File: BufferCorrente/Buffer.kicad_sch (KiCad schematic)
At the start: 6 parts

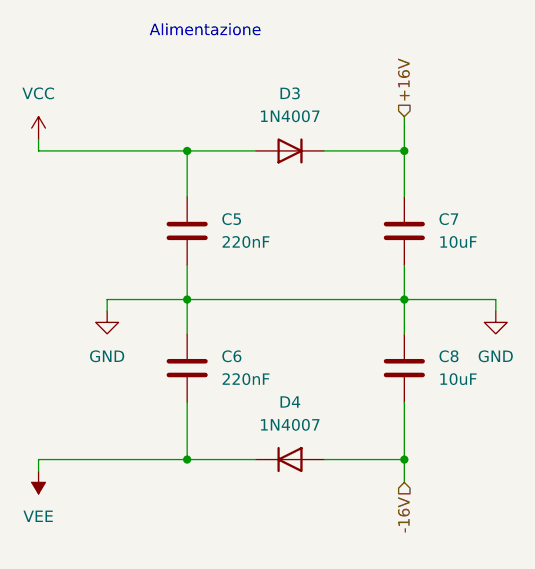
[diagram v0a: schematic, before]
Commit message: Aggiornata la PCB del buffer in corrente con coponenti SMD e groud plane
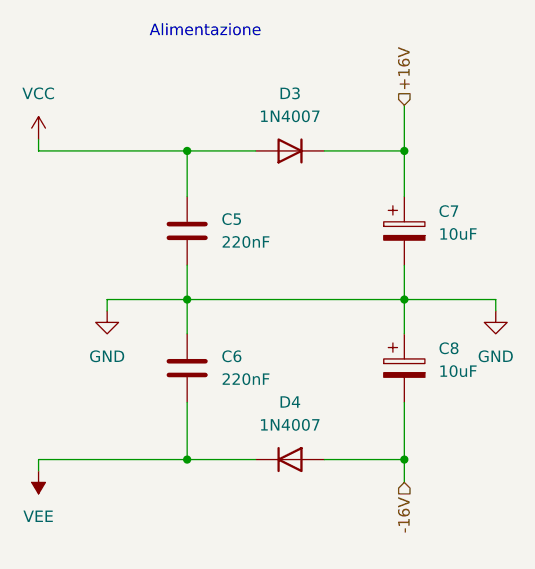
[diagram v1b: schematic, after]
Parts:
- removed C7, C8: 10uF, Capacitor_THT:C_Rect_L7.0mm_W2.0mm_P5.00mm, symbol Device:C
- added C7, C8: 10uF, Capacitor_Tantalum_SMD:CP_EIA-3528-21_Kemet-B, symbol Device:C_Polarized
- C5, C6: footprint Capacitor_THT:C_Rect_L7.0mm_W2.0mm_P5.00mm -> Capacitor_SMD:C_0201_0603Metric
- D3, D4: footprint Diode_THT:D_DO-41_SOD81_P10.16mm_Horizontal -> Diode_SMD:D_SMA
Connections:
- net +16V: now also C7.1
- net -16V: now also C8.2
- net GND: now also C7.2, C8.1
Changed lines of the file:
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@@
 	(wire
 		(pts
-			(xy 156.21 72.39) (xy 156.21 76.2)
+			(xy 156.21 71.12) (xy 156.21 76.2)
 		)
 		(stroke
@@
 		(shape input)
 		(at 156.21 113.03 270)
-		(fields_autoplaced yes)
 		(effects
 			(font
@@
 	(hierarchical_label "+16V"
 		(shape input)
-		(at 156.21 72.39 90)
-		(fields_autoplaced yes)
+		(at 156.21 71.12 90)
 		(effects
 			(font
@@
 	)
 	(symbol
-		(lib_id "Device:C")
+		(lib_id "Device:C_Polarized")
 		(at 156.21 85.09 0)
 		(unit 1)
@@
 		(fields_autoplaced yes)
 		(property "Reference" "C7"
-			(at 160.02 83.8199 0)
+			(at 160.02 82.9309 0)
 			(effects
 				(font
@@
 		)
 		(property "Value" "10uF"
-			(at 160.02 86.3599 0)
+			(at 160.02 85.4709 0)
 			(effects
 				(font
@@
 			)
 		)
-		(property "Footprint" "Capacitor_THT:C_Rect_L7.0mm_W2.0mm_P5.00mm"
+		(property "Footprint" "Capacitor_Tantalum_SMD:CP_EIA-3528-21_Kemet-B"
 			(at 157.1752 88.9 0)
 			(effects
@@
 			)
 		)
-		(property "Description" "Unpolarized capacitor"
+		(property "Description" "Polarized capacitor"
 			(at 156.21 85.09 0)
 			(effects
@@
 		)
 		(instances
-			(project "BufferCorrente"
+			(project ""
 				(path "/c4f3ca93-09e5-4832-b5c0-69d9bec68818/953b8590-3e03-4217-8c21-ab0eed29fe98"
 					(reference "C7")
@@
 			)
 		)
-		(property "Footprint" "Capacitor_THT:C_Rect_L7.0mm_W2.0mm_P5.00mm"
+		(property "Footprint" "Capacitor_SMD:C_0201_0603Metric"
 			(at 133.0452 88.9 0)
 			(effects
@@
 			)
 		)
-		(property "Footprint" "Capacitor_THT:C_Rect_L7.0mm_W2.0mm_P5.00mm"
+		(property "Footprint" "Capacitor_SMD:C_0201_0603Metric"
 			(at 133.0452 104.14 0)
 			(effects
@@
 	)
 	(symbol
-		(lib_id "Device:C")
+		(lib_id "Device:C_Polarized")
 		(at 156.21 100.33 0)
 		(unit 1)
@@
 		(fields_autoplaced yes)
 		(property "Reference" "C8"
-			(at 160.02 99.0599 0)
+			(at 160.02 98.1709 0)
 			(effects
 				(font
@@
 		)
 		(property "Value" "10uF"
-			(at 160.02 101.5999 0)
+			(at 160.02 100.7109 0)
 			(effects
 				(font
@@
 			)
 		)
-		(property "Footprint" "Capacitor_THT:C_Rect_L7.0mm_W2.0mm_P5.00mm"
+		(property "Footprint" "Capacitor_Tantalum_SMD:CP_EIA-3528-21_Kemet-B"
 			(at 157.1752 104.14 0)
 			(effects
@@
 			)
 		)
-		(property "Description" "Unpolarized capacitor"
+		(property "Description" "Polarized capacitor"
 			(at 156.21 100.33 0)
 			(effects
@@
 			)
 		)
-		(property "Footprint" "Diode_THT:D_DO-41_SOD81_P10.16mm_Horizontal"
+		(property "Footprint" "Diode_SMD:D_SMA"
 			(at 143.51 71.755 0)
 			(effects
@@
 			)
 		)
-		(property "Footprint" "Diode_THT:D_DO-41_SOD81_P10.16mm_Horizontal"
+		(property "Footprint" "Diode_SMD:D_SMA"
 			(at 143.51 114.935 0)
 			(effects
